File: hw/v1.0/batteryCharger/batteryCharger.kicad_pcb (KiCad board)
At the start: 2 copper layers, 40 x 40 mm, 27 parts, among them J1 PWR_IN, J2 USB_B_Micro, J3 USB_C_Receptacle_USB2.0, J4 BAT+, J5 BAT-, U1 LT3652EMSE

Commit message: Routing charger
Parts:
- moved R8 72.0 mm to (131.8, 64.0)
- moved C4 63.3 mm to (131.4, 68.4), turned to -90 degrees
- moved L1 61.4 mm to (122.0, 57.4)
- moved D3 53.3 mm to (121.1, 65.8)
- moved C3 48.6 mm to (133.2, 59.8), turned to 90 degrees
- moved D4 45.1 mm to (117.6, 70.2), turned to -90 degrees
- moved U1 5.81 mm to (121.4, 71.0), turned to 90 degrees
- moved D2 2.89 mm to (117.0, 85.0)
- moved D1 2.06 mm to (123.0, 85.0)

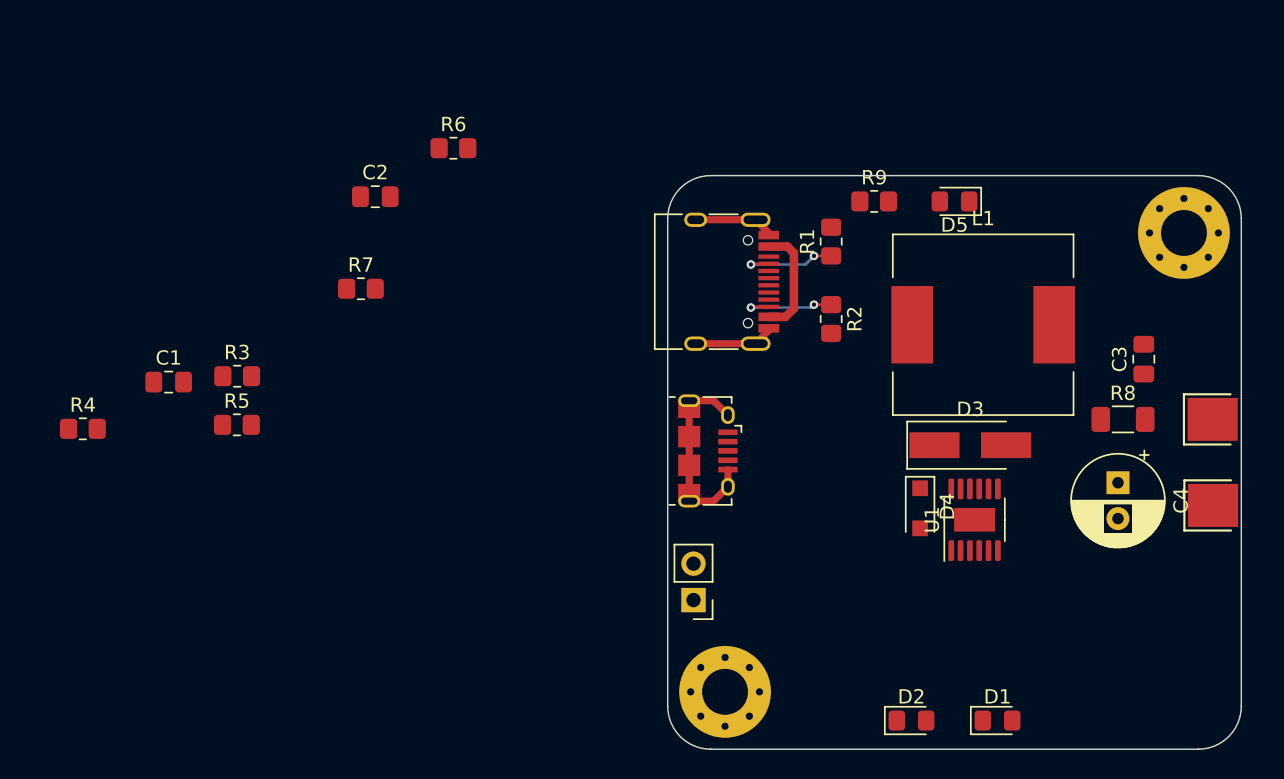
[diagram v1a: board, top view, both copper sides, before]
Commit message: Finish routing chargerBoard
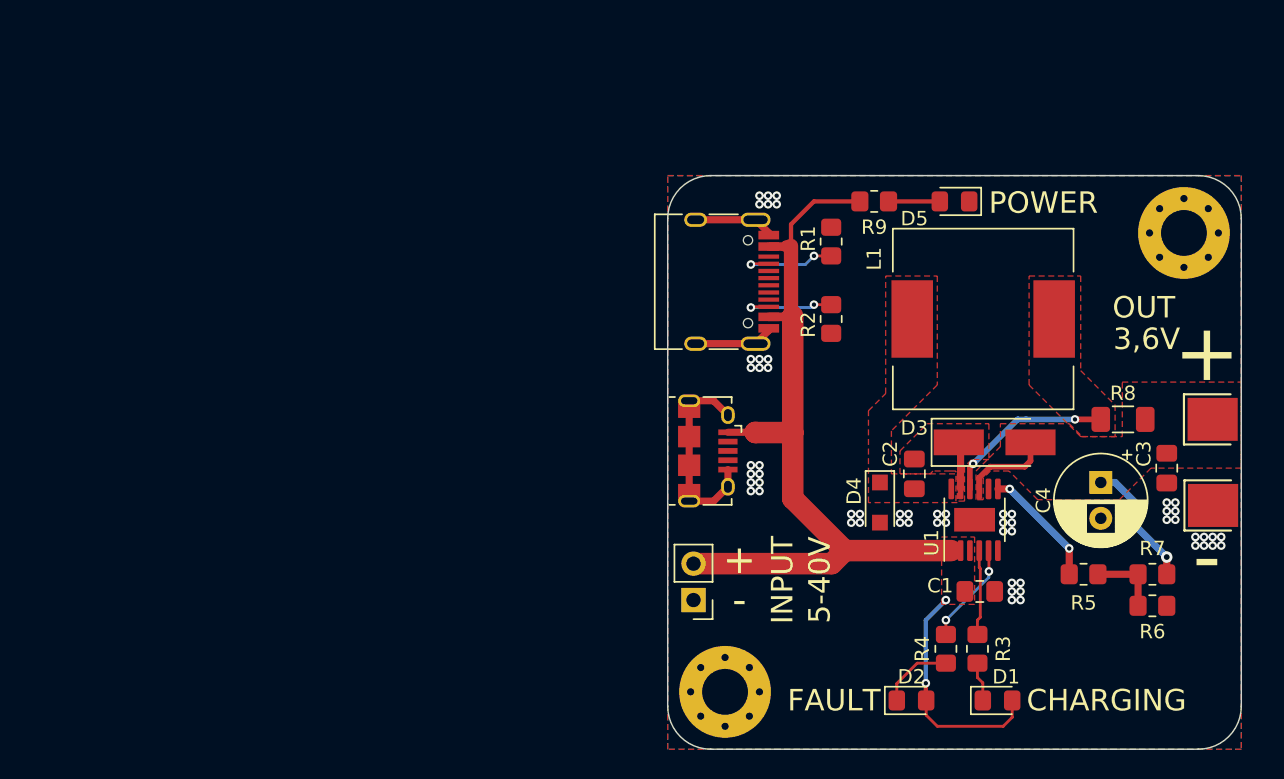
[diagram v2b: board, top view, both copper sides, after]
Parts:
- moved R4 62.1 mm to (119.4, 80.0), turned to 90 degrees
- moved R5 60.0 mm to (129.0, 74.8)
- moved R7 59.5 mm to (133.8, 77.0)
- moved C1 58.4 mm to (121.8, 76.0)
- moved R6 57.1 mm to (133.8, 74.8), turned to 180 degrees
- moved R3 55.0 mm to (121.6, 80.0), turned to 90 degrees
- moved C2 42.3 mm to (117.2, 67.8), turned to 90 degrees
- moved C3 7.77 mm to (134.8, 67.4), turned to -90 degrees
- moved D4 2.83 mm to (114.8, 69.8)
- moved D3 1.71 mm to (122.8, 65.6)
- moved D1 1.40 mm to (123.0, 83.6)
- moved D2 1.40 mm to (117.0, 83.6)
- moved C4 1.20 mm to (130.2, 68.4)
- moved L1 0.40 mm to (122.0, 57.0)
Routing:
- net VCC: track 7.81 -> 72.1 mm, vias 0 -> 2
- net Net-(C3-Pad1): track 0.00 -> 15.0 mm, vias 0 -> 1
- net Net-(L1-Pad2): track 0.00 -> 12.0 mm, vias 0 -> 2
- net Net-(R5-Pad1): track 0.00 -> 8.49 mm, vias 0 -> 2
- net Net-(R4-Pad2): track 0.00 -> 7.10 mm, vias 0 -> 2
- net Net-(R3-Pad2): track 0.00 -> 5.96 mm
- net Net-(D2-Pad1): track 0.00 -> 5.19 mm
- net Net-(R5-Pad2): track 0.00 -> 5.00 mm
- net Net-(D5-Pad2): track 0.00 -> 3.57 mm
- net Net-(C2-Pad2): track 0.00 -> 3.30 mm
- net Net-(D1-Pad1): track 0.00 -> 2.76 mm
- net GND: vias 0 -> 58
- added copper zone on B.Cu, net GND
- added copper zone on F.Cu, net GND
- added copper zone on F.Cu, net Net-(C2-Pad1)
- added copper zone on F.Cu, net Net-(C2-Pad2)
- added copper zone on F.Cu, net Net-(C3-Pad1)
- added copper zone on F.Cu, net Net-(L1-Pad2)
- added copper zone on F.Cu, net VCC
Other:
- board text added: "+"
- board text added: "-"
- board text added: "3,6V"
- board text added: "5-40V"
- board text added: "CHARGING"
- board text added: "FAULT"
- board text added: "INPUT"
- board text added: "OUT"
- board text added: "POWER"
- board text added: "batteryCharger v1.0 02/22 MAK"

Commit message: Tweak silkscreen at mainBoard, add MPPT option to batteryCharger
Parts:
- added JP1: MPPT EN, Jumper:SolderJumper-3_P1.3mm_Open_RoundedPad1.0x1.5mm_NumberLabels, F.Cu at (114.8, 75.6)
- added R10: R, Resistor_SMD:R_0805_2012Metric_Pad1.20x1.40mm_HandSolder, F.Cu at (114.4, 78.2)
- added R11: R, Resistor_SMD:R_0805_2012Metric_Pad1.20x1.40mm_HandSolder, F.Cu at (112.4, 80.2)
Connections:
- U1 pad 2: VCC -> Net-(U1-Pad2)
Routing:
- net VCC: track 72.1 -> 82.2 mm
- net Net-(U1-Pad2): track 0.00 -> 8.06 mm, vias 0 -> 2
- net Net-(JP1-Pad1): track 0.00 -> 4.64 mm
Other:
- board text added: "JLCJLCJLCJLC"
- board text added: "MPPT"

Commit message: Finished v1.0, mainBoard, batteryCharger
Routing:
- net VCC: track 82.2 -> 93.1 mm
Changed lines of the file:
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@@
   (net 25 "unconnected-(U1-Pad8)")
   (net 26 "Net-(JP1-Pad1)")
-  (net 27 "Net-(U1-Pad2)")
+  (net 27 "Net-(JP1-Pad2)")
   (footprint "Capacitor_THT:CP_Radial_D6.3mm_P2.50mm" (layer "F.Cu")
     (at 130.2 68.4 -90)
@@
       ))
     (pad "2" smd rect (at 0 0) (size 1 1.5) (layers "F.Cu" "F.Mask")
-      (net 27 "Net-(U1-Pad2)") (pinfunction "C") (pintype "passive"))
+      (net 27 "Net-(JP1-Pad2)") (pinfunction "C") (pintype "passive"))
     (pad "3" smd custom (at 1.3 0) (size 1 0.5) (layers "F.Cu" "F.Mask")
       (net 1 "VCC") (pinfunction "B") (pintype "passive") (zone_connect 2)
@@
       (net 1 "VCC") (pinfunction "VIN") (pintype "power_in"))
     (pad "2" smd roundrect (at -2.15 -0.975 90) (size 1.45 0.4) (layers "F.Cu" "F.Paste" "F.Mask") (roundrect_rratio 0.25)
-      (net 27 "Net-(U1-Pad2)") (pinfunction "VIN_REG") (pintype "input"))
+      (net 27 "Net-(JP1-Pad2)") (pinfunction "VIN_REG") (pintype "input"))
     (pad "3" smd roundrect (at -2.15 -0.325 90) (size 1.45 0.4) (layers "F.Cu" "F.Paste" "F.Mask") (roundrect_rratio 0.25)
       (net 1 "VCC") (pinfunction "~{SHDN}") (pintype "input"))
@@
     (effects (font (size 2 2) (thickness 0.4)))
   )
-  (segment (start 108.20377 51.953544) (end 108.257314 51.9) (width 0.75) (layer "F.Cu") (net 1))
-  (segment (start 107.045 56.85) (end 108.200428 56.85) (width 0.6) (layer "F.Cu") (net 1))
+  (segment (start 121.075 73.15) (end 121.075 74.075) (width 0.2) (layer "F.Cu") (net 1))
   (segment (start 118 83.575) (end 118.025 83.6) (width 0.3) (layer "F.Cu") (net 1))
   (segment (start 112.35 73.15) (end 108.719511 69.519511) (width 1.5) (layer "F.Cu") (net 1))
+  (segment (start 107.045 56.85) (end 109.282924 56.85) (width 0.6) (layer "F.Cu") (net 1))
+  (segment (start 109.282924 56.85) (end 109.316462 56.883538) (width 0.6) (layer "F.Cu") (net 1))
   (segment (start 101.8 74.06) (end 111.44 74.06) (width 1.5) (layer "F.Cu") (net 1))
+  (segment (start 121.075 74.075) (end 121.2 74.2) (width 0.2) (layer "F.Cu") (net 1))
   (segment (start 118.8 85.4) (end 123.4 85.4) (width 0.2) (layer "F.Cu") (net 1))
   (segment (start 113.4 48.8) (end 110.2 48.8) (width 0.3) (layer "F.Cu") (net 1))
-  (segment (start 108.200428 56.85) (end 108.20176 56.851332) (width 0.6) (layer "F.Cu") (net 1))
   (segment (start 116.1 75.6) (end 116.1 76.5) (width 0.3) (layer "F.Cu") (net 1))
-  (segment (start 108.719511 64.919511) (end 108.719511 56.8) (width 1.5) (layer "F.Cu") (net 1))
+  (segment (start 109.316462 53.066236) (end 109.316462 56.883538) (width 0.6) (layer "F.Cu") (net 1))
   (segment (start 121.075 75.65) (end 120.725 76) (width 0.3) (layer "F.Cu") (net 1))
+  (segment (start 108.20377 51.953544) (end 109.316462 53.066236) (width 0.6) (layer "F.Cu") (net 1))
   (segment (start 116.1 76.5) (end 115.4 77.2) (width 0.3) (layer "F.Cu") (net 1))
   (segment (start 118 82.4) (end 118 83.575) (width 0.3) (layer "F.Cu") (net 1))
+  (segment (start 121.2 75.525) (end 120.725 76) (width 0.2) (layer "F.Cu") (net 1))
   (segment (start 108.6 50.4) (end 108.6 51.9) (width 0.3) (layer "F.Cu") (net 1))
   (segment (start 115.4 77.2) (end 115.4 78.2) (width 0.3) (layer "F.Cu") (net 1))
   (segment (start 110.2 48.8) (end 108.6 50.4) (width 0.3) (layer "F.Cu") (net 1))
   (segment (start 108.200226 51.95) (end 108.20377 51.953544) (width 0.6) (layer "F.Cu") (net 1))
+  (segment (start 112.35 73.15) (end 109.316462 70.116462) (width 1.5) (layer "F.Cu") (net 1))
   (segment (start 111.44 74.06) (end 112.35 73.15) (width 1.5) (layer "F.Cu") (net 1))
-  (segment (start 108.20176 56.851332) (end 108.253092 56.8) (width 0.75) (layer "F.Cu") (net 1))
+  (segment (start 109.316462 70.116462) (end 109.316462 56.883538) (width 1.5) (layer "F.Cu") (net 1))
   (segment (start 108.719511 69.519511) (end 108.719511 64.919511) (width 1.5) (layer "F.Cu") (net 1))
   (segment (start 119.4 75.6) (end 119.8 76) (width 0.3) (layer "F.Cu") (net 1))
   (segment (start 106.1 64.9) (end 106.119511 64.919511) (width 1.5) (layer "F.Cu") (net 1))
   (segment (start 123.4 85.4) (end 124.025 84.775) (width 0.2) (layer "F.Cu") (net 1))
+  (segment (start 121.2 74.2) (end 121.2 75.525) (width 0.2) (layer "F.Cu") (net 1))
   (segment (start 116.1 75.6) (end 119.4 75.6) (width 0.3) (layer "F.Cu") (net 1))
   (segment (start 107.045 51.95) (end 108.200226 51.95) (width 0.6) (layer "F.Cu") (net 1))
-  (segment (start 108.6 56.7) (end 108.5 56.8) (width 1) (layer "F.Cu") (net 1))
-  (segment (start 108.257314 51.9) (end 108.6 51.9) (width 0.75) (layer "F.Cu") (net 1))
-  (segment (start 108.253092 56.8) (end 108.5 56.8) (width 0.75) (layer "F.Cu") (net 1))
   (segment (start 118.025 84.625) (end 118.8 85.4) (width 0.2) (layer "F.Cu") (net 1))
-  (segment (start 121.075 73.15) (end 121.075 75.65) (width 0.3) (layer "F.Cu") (net 1))
-  (segment (start 108.6 51.9) (end 108.6 56.7) (width 1) (layer "F.Cu") (net 1))
   (segment (start 118.025 83.6) (end 118.025 84.625) (width 0.2) (layer "F.Cu") (net 1))
   (segment (start 112.35 73.15) (end 119.27548 73.15) (width 1.5) (layer "F.Cu") (net 1))
